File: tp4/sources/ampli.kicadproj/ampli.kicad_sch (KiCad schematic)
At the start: 11 parts, among them J101 AUDIO_IN, J102 DIFF_AUDIO_IN, J103 P_POW, J104 N_POW, J105 P_POW, J106 AUDIO_OUT, J107 N_POW, J108 P_POW, J109 AUDIO_IN, J110 N_POW, J111 AUDIO_OUT

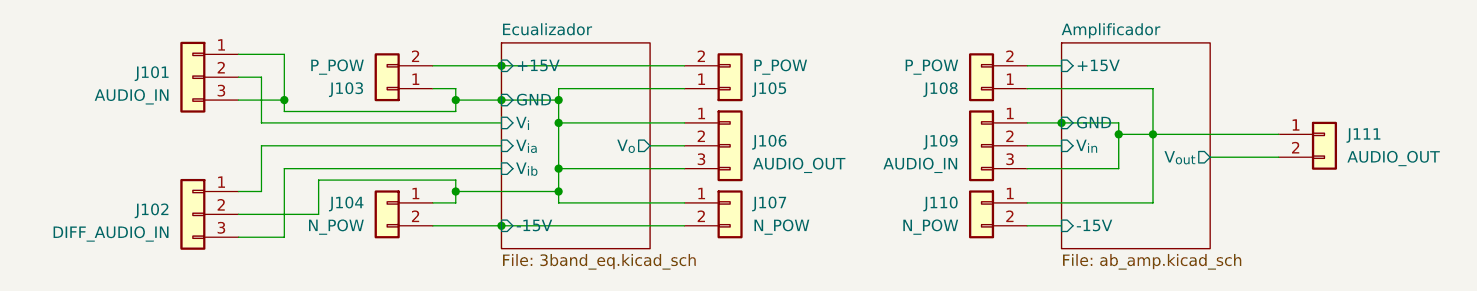
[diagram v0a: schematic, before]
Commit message: tp4: Agrega pcb y actualiza simulaciones
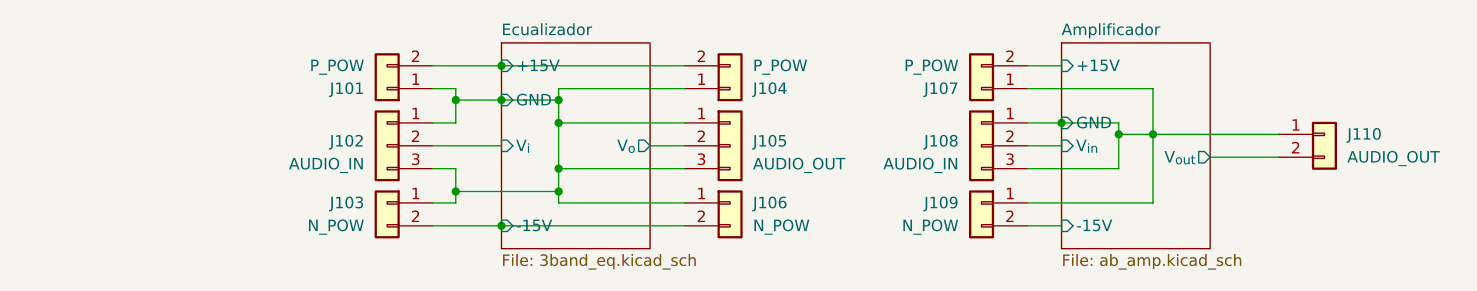
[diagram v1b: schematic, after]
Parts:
- removed J102: DIFF_AUDIO_IN, symbol Connector_Generic:Conn_01x03
- J101: renamed from J103; footprint Connector:Tag-Connect_TC2030-IDC-FP_2x03_P1.27mm_Vertical -> Connector_PinHeader_2.54mm:PinHeader_1x02_P2.54mm_Vertical
- J102: renamed from J101; footprint (none) -> Connector_PinHeader_2.54mm:PinHeader_1x03_P2.54mm_Vertical
- J103: renamed from J104; footprint Connector:Tag-Connect_TC2030-IDC-FP_2x03_P1.27mm_Vertical -> Connector_PinHeader_2.54mm:PinHeader_1x02_P2.54mm_Vertical
- J104: renamed from J105; footprint Connector:Tag-Connect_TC2030-IDC-FP_2x03_P1.27mm_Vertical -> Connector_PinHeader_2.54mm:PinHeader_1x02_P2.54mm_Vertical
- J105: renamed from J106; footprint (none) -> Connector_PinHeader_2.54mm:PinHeader_1x03_P2.54mm_Vertical
- J106: renamed from J107; footprint Connector:Tag-Connect_TC2030-IDC-FP_2x03_P1.27mm_Vertical -> Connector_PinHeader_2.54mm:PinHeader_1x02_P2.54mm_Vertical
- J107: renamed from J108; footprint Connector:Tag-Connect_TC2030-IDC-FP_2x03_P1.27mm_Vertical -> Connector_PinHeader_2.54mm:PinHeader_1x02_P2.54mm_Vertical
- J108: renamed from J109; footprint (none) -> Connector_PinHeader_2.54mm:PinHeader_1x03_P2.54mm_Vertical
- J109: renamed from J110; footprint Connector:Tag-Connect_TC2030-IDC-FP_2x03_P1.27mm_Vertical -> Connector_PinHeader_2.54mm:PinHeader_1x02_P2.54mm_Vertical
- J110: renamed from J111; footprint Connector:Tag-Connect_TC2030-IDC-FP_2x03_P1.27mm_Vertical -> TerminalBlock_Phoenix:TerminalBlock_Phoenix_MKDS-1,5-2-5.08_1x02_P5.08mm_Horizontal
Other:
- sheet Ecualizador ports: added none; removed V_{ia}, V_{ib}
- moved on the sheet: J102
